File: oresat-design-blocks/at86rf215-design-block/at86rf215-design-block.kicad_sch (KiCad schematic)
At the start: 19 parts, among them J1 Conn_01x04, J2 Conn_01x04, J3 Conn_01x07, J5 Conn_01x10, U2 AT86RF215

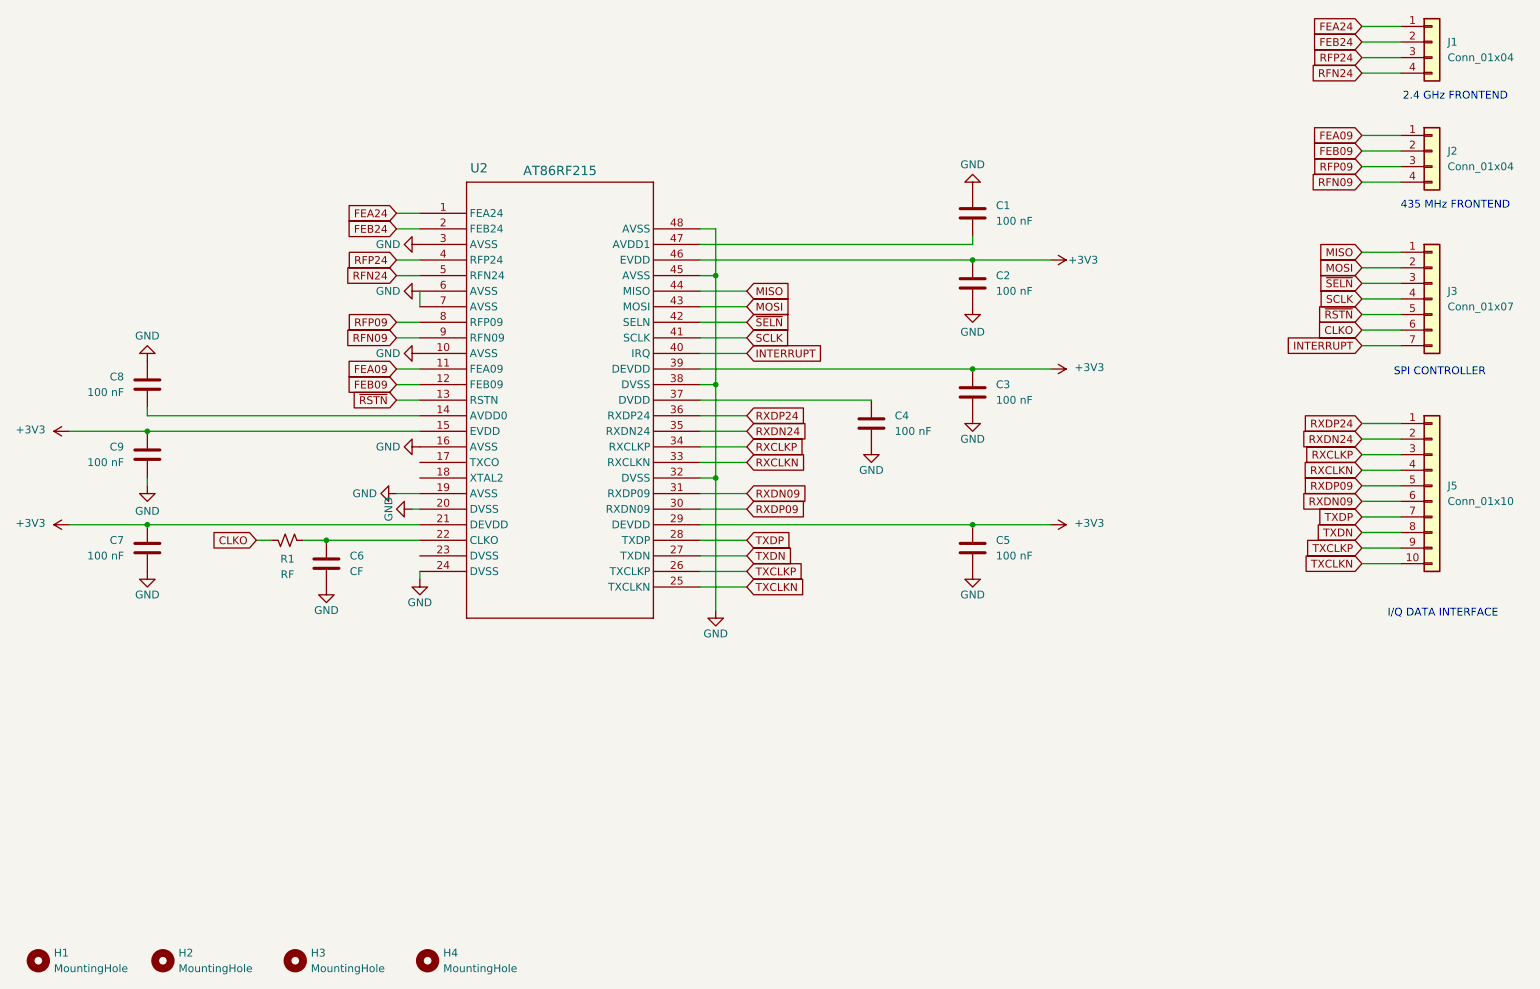
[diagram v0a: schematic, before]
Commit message: Added crystal, CLK, RSTN, and 2.4 GHz circuitry. Split schematic into Power and RF sections. Added 2450FB15A balun filter into oresat libraries
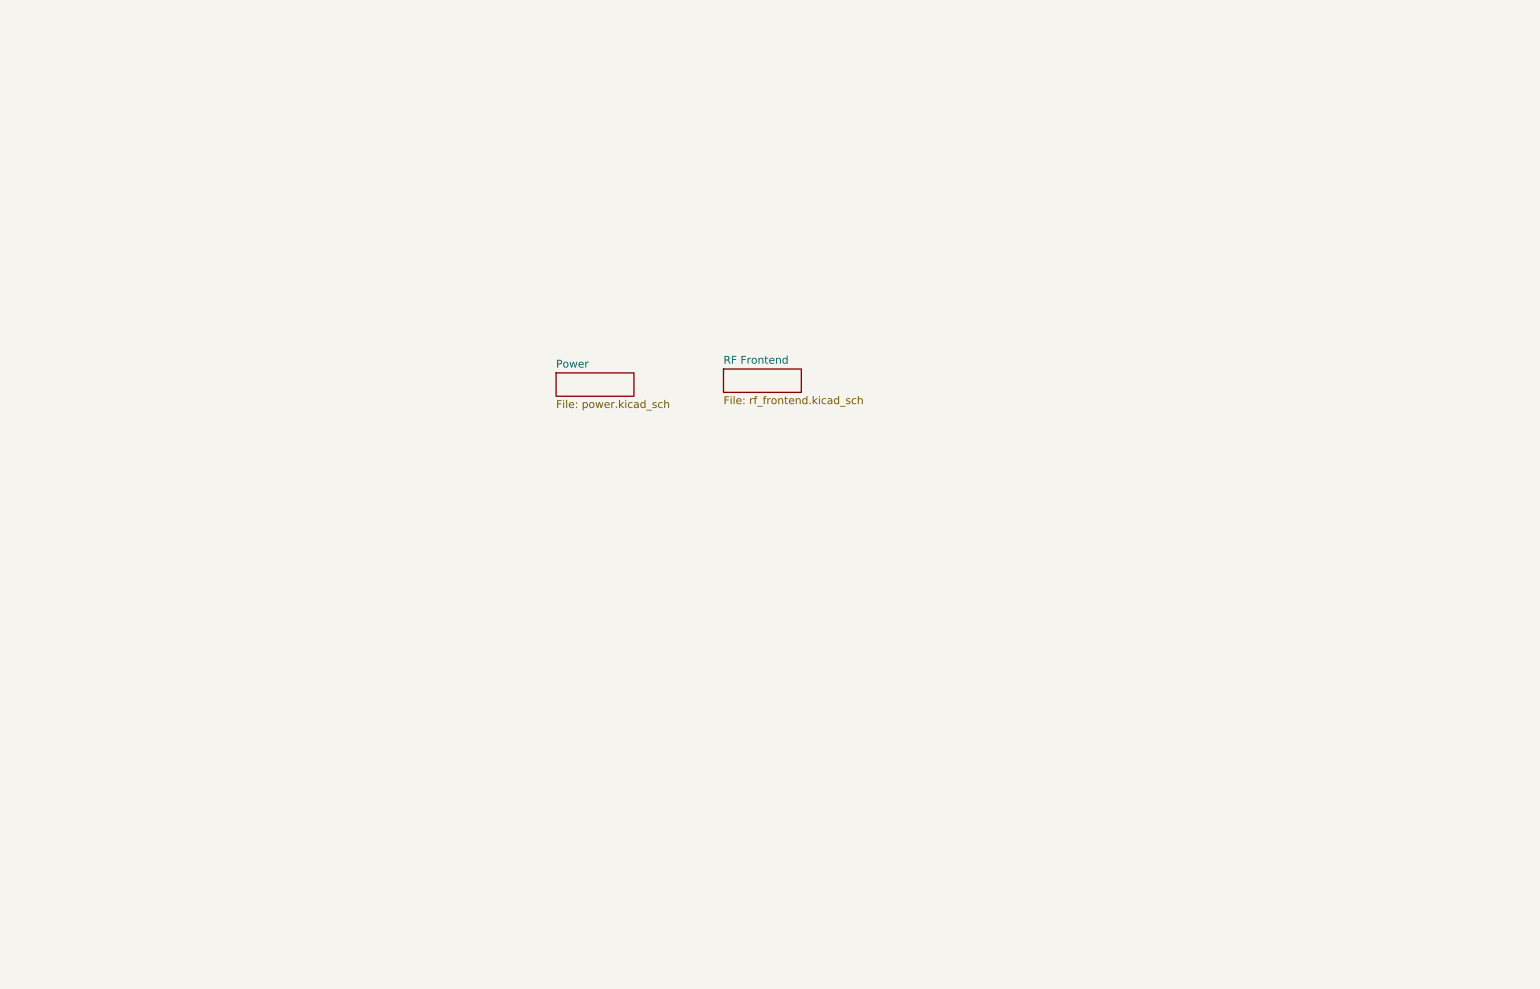
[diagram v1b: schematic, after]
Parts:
- removed C1, C2, C3, C4, C5, C7, C8, C9: 100 nF, symbol Device:C
- removed C6: CF, symbol Device:C
- removed H1, H2, H3, H4: MountingHole, symbol Mechanical:MountingHole
- removed J1, J2: Conn_01x04, symbol Connector_Generic:Conn_01x04
- removed J3: Conn_01x07, symbol Connector_Generic:Conn_01x07
- removed J5: Conn_01x10, symbol Connector_Generic:Conn_01x10
- removed R1: RF, symbol Device:R_Small_US
- removed U2: AT86RF215, Package_DFN_QFN:QFN-48-1EP_7x7mm_P0.5mm_EP5.6x5.6mm, symbol oresat-ics:AT86RF215
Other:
- added sheet Power (power.kicad_sch)
- added sheet RF Frontend (rf_frontend.kicad_sch)
- note removed: "2.4 GHz FRONTEND"
- note removed: "435 MHz FRONTEND"
- note removed: "I/Q DATA INTERFACE"
- note removed: "SPI CONTROLLER"

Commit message: First design review of AT86 eval board. Added 5V to 3.3V LDO with low noise, added USB C port, and found a Balun for UHF and L band.
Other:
- company: (none) -> Portland State Aerospace Society
- title: (none) -> OreSat AT86RF215 Evaluation Board
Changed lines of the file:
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@@
 	(generator "eeschema")
 	(generator_version "9.0")
-	(paper "A4")
+	(paper "B")
+	(title_block
+		(title "OreSat AT86RF215 Evaluation Board")
+		(date "2025-12-16")
+		(rev "1.0")
+		(company "Portland State Aerospace Society")
+	)
 	(sheet
 		(at 117.475 85.725)

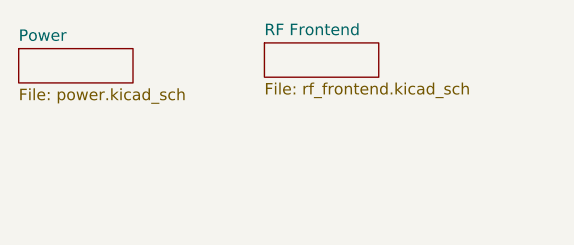
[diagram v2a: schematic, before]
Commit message: Design review and cleanup of AT86RF215 eval board; ready for layout.
Added footprints to SMAs, made a symbol for a balun, cleaned up and renamed schematic. Added terminal block for power just cause.
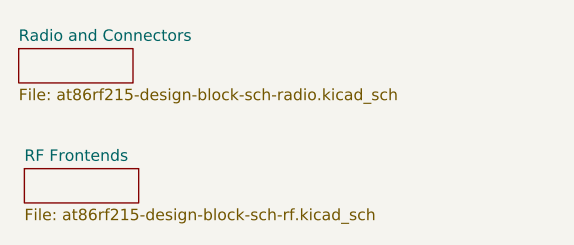
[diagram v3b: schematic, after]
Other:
- sheet Power renamed Radio and Connectors
- sheet RF Frontend renamed RF Frontends
- sheet RF Frontends: file rf_frontend.kicad_sch -> at86rf215-design-block-sch-rf.kicad_sch
- sheet Radio and Connectors: file power.kicad_sch -> at86rf215-design-block-sch-radio.kicad_sch
